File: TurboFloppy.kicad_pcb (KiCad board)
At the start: 2 copper layers, 87.9 x 99.7 mm, 20 parts, among them CN1 EXPANSION_PORT, CN2 SOCKET_28PIN, CN3 PIN_HEADER_28PIN, Q1 BC547, U1 8255, U2 74LS30, U4 74LS27, U5 74LS10

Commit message: Who knows?
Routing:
- net /r_~{w}: track 165.4 -> 161.8 mm
- net /~{irq}: track 99.0 -> 96.5 mm
- net +5V: track 262.5 -> 260.4 mm
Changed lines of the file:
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@@
 	(paper "A4")
 	(title_block
+		(title "Intel 8255 Interface for the Commodore 16, 116 and Plus/4")
 		(date "2024-07-14")
 		(rev "1git")
 		(company "SukkoPera")
+		(comment 1 "Based on the article published in Rádiótechnika 1988/12 by Ferenc Garay and Dr. János Rohonczy")
+		(comment 2 "http://plus4world.powweb.com/publications/Radiotechnika_1988_december")
 		(comment 3 "Licensed under CC BY-NC-SA 4.0")
 	)
@@
 			(drillshape 0)
 			(scaleselection 1)
-			(outputdirectory "")
+			(outputdirectory "gerbers")
 		)
 	)
@@
 	)
 	(segment
-		(start 124.841 99.568)
-		(end 129.032 99.568)
-		(width 0.25)
-		(layer "F.Cu")
-		(net 19)
-	)
-	(segment
 		(start 128.548 126.8095)
-		(end 128.548 138.828)
+		(end 130.6068 124.7507)
 		(width 0.25)
 		(layer "F.Cu")
@@
 	)
 	(segment
-		(start 129.032 99.568)
-		(end 130.6068 101.1428)
+		(start 128.548 138.828)
+		(end 128.548 126.8095)
 		(width 0.25)
 		(layer "F.Cu")
@@
 	)
 	(segment
-		(start 124.841 68.199)
-		(end 124.841 61.849)
+		(start 130.6068 101.2698)
+		(end 112.268 82.931)
 		(width 0.25)
 		(layer "F.Cu")
@@
 	(segment
 		(start 124.841 68.199)
-		(end 122.301 70.739)
+		(end 124.841 61.849)
 		(width 0.25)
 		(layer "F.Cu")
@@
 	(segment
 		(start 130.6068 124.7507)
-		(end 128.548 126.8095)
+		(end 130.6068 101.2698)
 		(width 0.25)
 		(layer "F.Cu")
@@
 	)
 	(segment
-		(start 130.6068 101.1428)
-		(end 130.6068 124.7507)
-		(width 0.25)
-		(layer "F.Cu")
-		(net 19)
-	)
-	(segment
-		(start 112.268 86.995)
-		(end 124.841 99.568)
+		(start 124.841 68.199)
+		(end 122.301 70.739)
 		(width 0.25)
 		(layer "F.Cu")
@@
 	)
 	(via
-		(at 112.268 86.995)
+		(at 112.268 82.931)
 		(size 0.6)
 		(drill 0.4)
@@
 	(segment
 		(start 112.268 70.739)
-		(end 112.268 86.995)
+		(end 112.268 82.931)
 		(width 0.25)
 		(layer "B.Cu")
@@
 	)
 	(segment
+		(start 110.871 83.439)
+		(end 128.651 101.219)
+		(width 0.5)
+		(layer "F.Cu")
+		(net 26)
+	)
+	(segment
 		(start 113.665 54.229)
 		(end 117.221 54.229)
@@
 	)
 	(segment
-		(start 110.871 81.661)
-		(end 110.871 78.359)
-		(width 0.5)
-		(layer "F.Cu")
-		(net 26)
-	)
-	(segment
-		(start 125.349 101.219)
-		(end 123.571 99.441)
-		(width 0.5)
-		(layer "F.Cu")
-		(net 26)
-	)
-	(segment
-		(start 110.871 78.359)
-		(end 113.411 75.819)
-		(width 0.5)
-		(layer "F.Cu")
-		(net 26)
-	)
-	(segment
 		(start 124.548 131.445)
 		(end 124.548 129.032)
@@
 	)
 	(segment
-		(start 110.871 86.741)
-		(end 123.571 99.441)
+		(start 113.411 75.819)
+		(end 110.871 78.359)
 		(width 0.5)
 		(layer "F.Cu")
@@
 	)
 	(segment
-		(start 128.651 101.219)
-		(end 125.349 101.219)
-		(width 0.5)
-		(layer "F.Cu")
-		(net 26)
-	)
-	(segment
-		(start 110.871 81.661)
-		(end 110.871 86.741)
-		(width 0.5)
-		(layer "F.Cu")
-		(net 26)
-	)
-	(segment
 		(start 113.411 75.819)
 		(end 110.871 73.279)
@@
 	)
 	(segment
+		(start 110.871 78.359)
+		(end 110.871 83.439)
+		(width 0.5)
+		(layer "F.Cu")
+		(net 26)
+	)
+	(segment
 		(start 110.871 57.023)
 		(end 113.665 54.229)
@@
 	)
 	(segment
-		(start 127.381 68.199)
-		(end 127.254 68.326)
-		(width 0.5)
-		(layer "B.Cu")
-		(net 26)
-	)
-	(segment
 		(start 127.254 72.263)
 		(end 126.111 73.406)
@@
 	)
 	(segment
-		(start 124.714 98.552)
-		(end 111.633 85.471)
+		(start 131.191 100.838)
+		(end 111.633 81.28)
 		(width 0.25)
 		(layer "F.Cu")
@@
 	(segment
 		(start 131.191 125.73)
-		(end 131.191 100.584)
-		(width 0.25)
-		(layer "F.Cu")
-		(net 33)
-	)
-	(segment
-		(start 131.191 100.584)
-		(end 129.159 98.552)
+		(end 131.191 100.838)
 		(width 0.25)
 		(layer "F.Cu")
@@
 	)
 	(segment
-		(start 129.159 98.552)
-		(end 124.714 98.552)
+		(start 130.548 138.828)
+		(end 130.548 126.373)
 		(width 0.25)
 		(layer "F.Cu")
@@
 		(net 33)
 	)
-	(segment
-		(start 130.548 138.828)
-		(end 130.548 126.373)
-		(width 0.25)
-		(layer "F.Cu")
-		(net 33)
-	)
 	(via
-		(at 111.633 85.471)
+		(at 111.633 81.28)
 		(size 0.6)
 		(drill 0.4)
@@
 	)
 	(segment
-		(start 111.633 85.471)
-		(end 111.633 67.437)
-		(width 0.25)
-		(layer "B.Cu")
-		(net 33)
-	)
-	(segment
-		(start 107.315 63.119)
-		(end 107.061 63.119)
-		(width 0.25)
-		(layer "B.Cu")
-		(net 33)
-	)
-	(segment
 		(start 167.64 45.339)
 		(end 170.561 48.26)
@@
 	)
 	(segment
-		(start 107.061 63.119)
-		(end 107.823 63.119)
+		(start 111.633 81.28)
+		(end 111.633 67.437)
 		(width 0.25)
 		(layer "B.Cu")
@@
 	)
 	(segment
-		(start 124.841 78.74)
+		(start 124.841 87.63)
 		(end 124.841 77.089)
 		(width 0.25)
@@
 		(width 0.25)
 		(layer "B.Cu")
-		(net 69)
-	)
-	(segment
-		(start 124.841 78.74)
-		(end 124.841 87.63)
-		(width 0.25)
-		(layer "B.Cu")

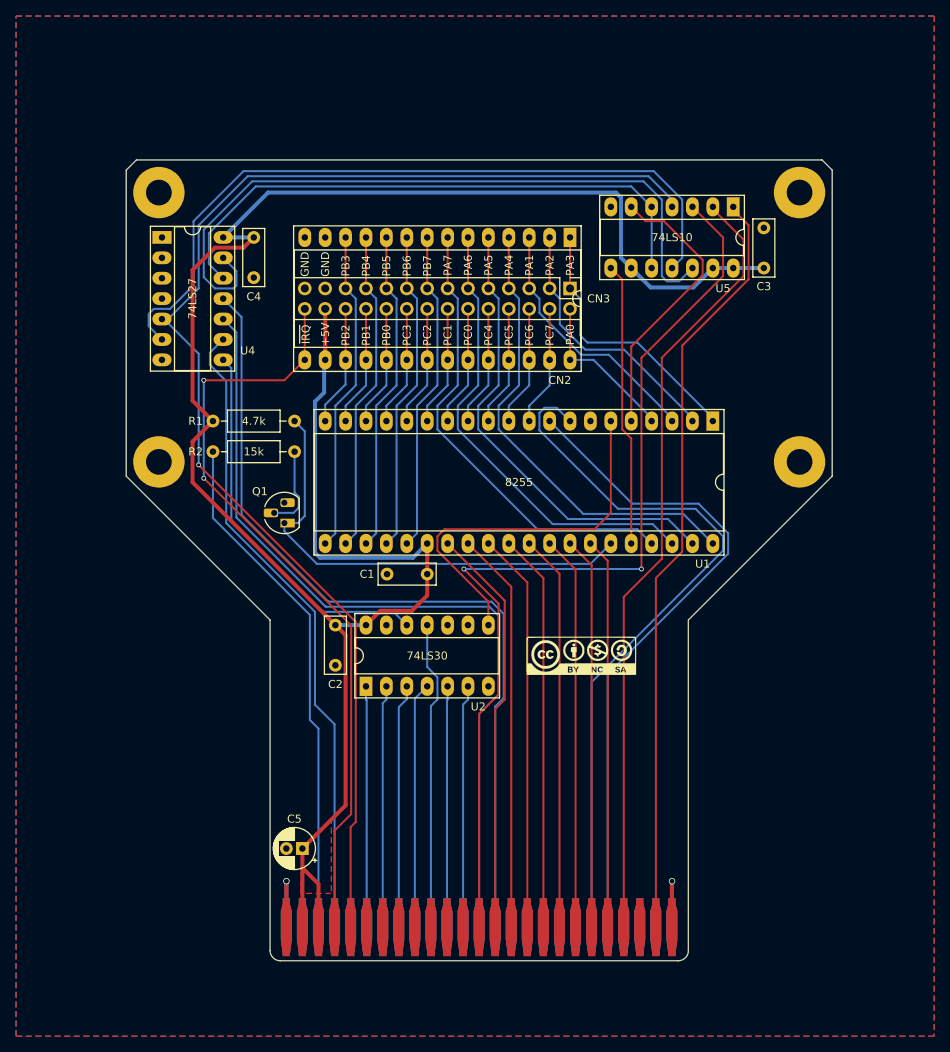
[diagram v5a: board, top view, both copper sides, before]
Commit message: Replace all logic with a GAL and make muuuuch smaller
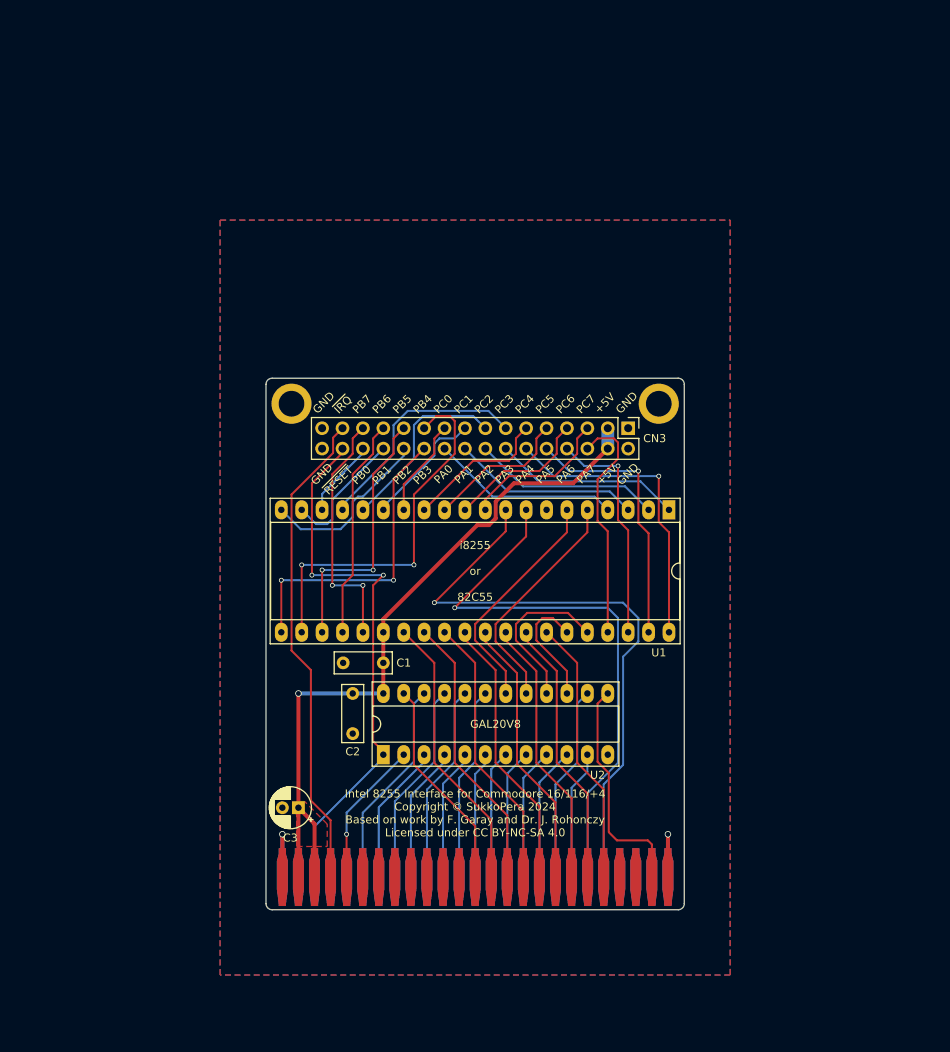
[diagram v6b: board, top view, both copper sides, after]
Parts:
- removed C4: 100n, Capacitor_THT:C_Disc_D7.0mm_W2.5mm_P5.00mm
- removed C5: 47n, Capacitor_THT:CP_Radial_D5.0mm_P2.00mm
- removed CN2: SOCKET_28PIN, Package_DIP:DIP-28_W15.24mm_Socket_LongPads
- removed H3, H4: SCREW HOLE, MountingHole:MountingHole_3.2mm_M3_Pad
- removed Q1: BC547, Package_TO_SOT_THT:TO-92_HandSolder
- removed R1: 4.7k, Resistor_THT:R_Axial_DIN0207_L6.3mm_D2.5mm_P10.16mm_Horizontal
- removed R2: 15k, Resistor_THT:R_Axial_DIN0207_L6.3mm_D2.5mm_P10.16mm_Horizontal
- removed U4: 74LS27, Package_DIP:DIP-14_W7.62mm_Socket_LongPads
- removed U5: 74LS10, Package_DIP:DIP-14_W7.62mm_Socket_LongPads
- C3: value 100n -> 47n; footprint Capacitor_THT:C_Disc_D7.0mm_W2.5mm_P5.00mm -> Capacitor_THT:CP_Radial_D5.0mm_P2.00mm
- CN3: value PIN_HEADER_28PIN -> PIN_HEADER_32PIN; footprint Connector_PinHeader_2.54mm:PinHeader_2x14_P2.54mm_Vertical -> Connector_PinHeader_2.54mm:PinHeader_2x16_P2.54mm_Vertical
- U2: value 74LS30 -> GAL20V8; footprint Package_DIP:DIP-14_W7.62mm_Socket_LongPads -> Package_DIP:DIP-24_W7.62mm_Socket_LongPads
- V0: moved to B.Cu
- moved C3 88.7 mm to (124.0, 124.0), turned to 180 degrees
- moved H2 31.6 mm to (168.9, 73.7)
- moved H1 31.0 mm to (123.2, 73.7)
- moved V0 20.4 mm to (161.9, 125.2), turned to 180 degrees
- moved CN3 18.8 mm to (165.1, 76.7)
- moved C1 12.3 mm to (134.6, 105.9)
- moved U1 12.3 mm to (170.2, 86.9)
- moved C2 8.78 mm to (130.8, 109.7)
- moved U2 8.78 mm to (134.6, 117.3)
- moved CN1 6.26 mm to (146.1, 132.6)
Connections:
- CN1 pad 22: /aec -> unconnected-(CN1-AEC-Pad22)
- CN1 pad D: /~{ras} -> unconnected-(CN1-/RAS-PadD)
- CN3 pad 1: /pa3 -> GND
- CN3 pad 10: /pc4 -> /pa5
- CN3 pad 11: /pa6 -> /pc4
- CN3 pad 12: /pc0 -> /pa4
- CN3 pad 13: /pa7 -> /pc3
- CN3 pad 14: /pc1 -> /pa3
- CN3 pad 15: /pb7 -> /pc2
- CN3 pad 16: /pc2 -> /pa2
- CN3 pad 17: /pb6 -> /pc1
- CN3 pad 18: /pc3 -> /pa1
- CN3 pad 19: /pb5 -> /pc0
- CN3 pad 2: /pa0 -> GND
- CN3 pad 20: /pb0 -> /pa0
- CN3 pad 22: /pb1 -> /pb3
- CN3 pad 23: /pb3 -> /pb5
- CN3 pad 25: GND -> /pb6
- CN3 pad 26: +5V -> /pb1
- CN3 pad 27: GND -> /pb7
- CN3 pad 28: /~{irq} -> /pb0
- CN3 pad 3: /pa2 -> +5V
- CN3 pad 4: /pc7 -> +5V
- CN3 pad 5: /pa1 -> /pc7
- CN3 pad 6: /pc6 -> /pa7
- CN3 pad 7: /pa4 -> /pc6
- CN3 pad 8: /pc5 -> /pa6
- CN3 pad 9: /pa5 -> /pc5
- U1 pad 35: Net-(Q1-C) -> /reset
- U2 pad 1: /a15 -> /~{reset}
- U2 pad 10: (no net) -> /a4
- U2 pad 11: /a11 -> /a2
- U2 pad 12: Net-(U2-Pad12) -> GND
- U2 pad 13: (no net) -> /phi2
- U2 pad 14: +5V -> /a3
- U2 pad 2: /a14 -> /r_~{w}
- U2 pad 3: /a13 -> /a14
- U2 pad 6: /a9 -> /a8
- U2 pad 7: GND -> /a7
- U2 pad 8: /~{cs8255} -> /a6
- U2 pad 9: (no net) -> /a5
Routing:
- net +5V: track 260.4 -> 93.1 mm, vias 0 -> 1
- net /r_~{w}: track 161.8 -> 18.1 mm
- net /aec: track 97.2 -> 0.00 mm
- net /ba: track 120.4 -> 26.5 mm, vias 2 -> 0
- net Net-(U4-Pad6): track 92.8 -> 0.00 mm
- net Net-(U4-Pad13): track 89.6 -> 0.00 mm
- net /a7: track 105.1 -> 16.0 mm
- net /a8: track 102.9 -> 15.8 mm
- net /~{ras}: track 80.3 -> 0.00 mm
- net Net-(U4-Pad12): track 72.5 -> 0.00 mm
- net /phi2: track 94.9 -> 28.4 mm
- net Net-(Q1-C): track 59.6 -> 0.00 mm
- net Net-(U2-Pad12): track 47.6 -> 0.00 mm
- net /~{irq}: track 96.5 -> 60.5 mm, vias 2 -> 0
- net /pa6: track 58.0 -> 28.5 mm, vias 0 -> 1
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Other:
- board size 87.9 x 99.7 mm -> 52.1 x 66.2 mm
- board text added: "Intel 8255 Interface for Commodore 16/116/+4 Copyright © SukkoPera 2024 Based on work by F. Garay and Dr. J. Rohonczy Licensed under CC BY-NC-SA 4.0"
- board text added: "V2"
- board text added: "i8255 or 82C55"
- board text added: "~{RESET}"

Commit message: Final touches
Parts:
- C3: value 47n -> 47u
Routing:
- net +5V: track 93.1 -> 97.4 mm
- net /pb4: track 47.1 -> 43.2 mm, vias 2 -> 1
- net /a0: track 75.5 -> 72.3 mm
- net /pb3: track 38.4 -> 35.4 mm, vias 2 -> 1
- net /~{reset}: track 68.1 -> 66.3 mm
- net /pb0: track 9.15 -> 9.95 mm
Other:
- board text added: "GAL20V8 or GAL22V10"
- board text added: "i8255(A), 82C55(A), μPD8255A-x, etc..."
- board text removed: "i8255 or 82C55"

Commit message: (Very) Final touches Note project URL is still missing!
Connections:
- U2 pad 15: /reset -> /a5
- U2 pad 16: /~{wr8255} -> /a7
- U2 pad 17: /~{rd8255} -> /reset
- U2 pad 18: /~{cs8255} -> /~{wr8255}
- U2 pad 19: /a9 -> /~{rd8255}
- U2 pad 20: /a11 -> /~{cs8255}
- U2 pad 5: /a10 -> /a11
- U2 pad 6: /a8 -> /a10
- U2 pad 7: /a7 -> /a9
- U2 pad 8: /a6 -> /a8
- U2 pad 9: /a5 -> /a6
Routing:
- net /~{rd8255}: track 29.2 -> 41.8 mm, vias 0 -> 2
- net /~{cs8255}: track 29.2 -> 40.2 mm, vias 0 -> 2
- net /a7: track 16.0 -> 25.7 mm
- net /a5: track 16.4 -> 25.1 mm
- net /a1: track 70.1 -> 61.6 mm, vias 1 -> 3
- net /a11: track 24.8 -> 17.2 mm
- net /a9: track 24.2 -> 17.6 mm
- net /~{wr8255}: track 20.7 -> 26.6 mm, vias 0 -> 1
- net /reset: track 15.1 -> 20.6 mm, vias 0 -> 1
- net /a0: track 72.3 -> 66.9 mm, vias 1 -> 3
- net /a8: track 15.8 -> 17.9 mm
- net /a10: track 15.5 -> 17.4 mm
- net /a4: track 16.7 -> 15.6 mm
- net /pb0: track 9.95 -> 9.19 mm
